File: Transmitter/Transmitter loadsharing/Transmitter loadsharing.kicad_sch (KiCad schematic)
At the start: 115 parts, among them J1 Conn_Coaxial, J10 Conn_01x01, J11 Conn_01x01, J12 Conn_01x01, J13 Conn_01x01, J14 Conn_01x01, J15 Conn_01x01, J16 Conn_01x01, J17 Conn_Coaxial, J18 Conn_Coaxial, J19 Conn_Coaxial, J2 Conn_01x03, J20 Conn_01x01, J21 Conn_01x01, J22 Conn_01x01, J23 Conn_01x01, J24 Conn_01x01, J25 Conn_01x01, J3 Conn_01x03, J4 Conn_01x02_Socket, J5 Conn_01x02, J6 Conn_01x01, J7 Conn_01x02, J8 Conn_01x02_Socket, J9 Conn_01x01, U1 OPA3692IDBQR, U10 LT3094EMSE-PBF, U11 LT3094EMSE-PBF, U2 THS3091D, U3 THS3091D, U4 THS3091D, U5 THS3091D, U6 THS3091D, U7 THS3091D, U8 LT3045EMSE-PBF, U9 LT3045EMSE-PBF

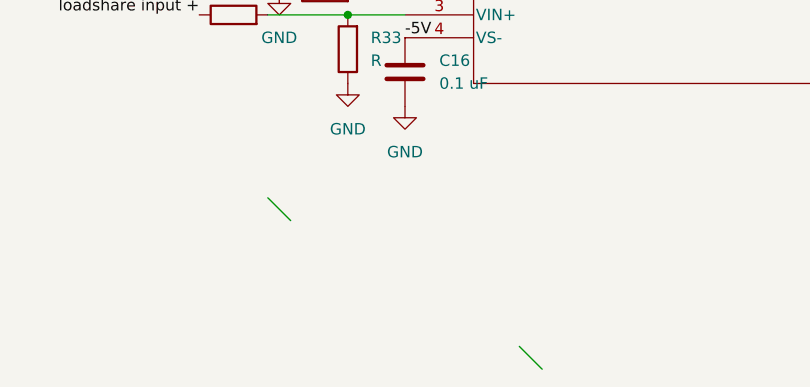
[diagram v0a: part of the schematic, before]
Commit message: Fixed spacing between ICs, tried to make traces the same length each of the loadsharing op-amps
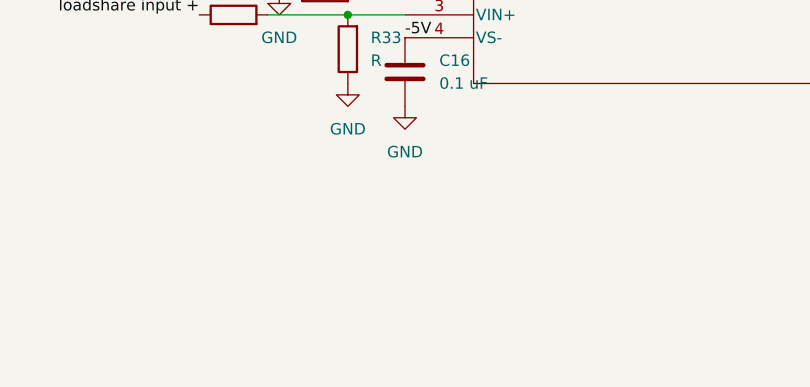
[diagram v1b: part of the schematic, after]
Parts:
- U2: footprint THS3091DDR:DDA8_2P28X2P28 -> D8
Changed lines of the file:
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@@
 		(at 336.55 107.95)
 	)
-	(bus_entry
-		(at 39.37 265.43)
-		(size 2.54 2.54)
-		(stroke
-			(width 0)
-			(type default)
-		)
-	)
-	(bus_entry
-		(at 67.31 281.94)
-		(size 2.54 2.54)
-		(stroke
-			(width 0)
-			(type default)
-		)
-	)
 	(wire
 		(pts
@@
 	)
 	(symbol
+		(lib_name "THS3091D_2")
 		(lib_id "THS3091:THS3091D")
 		(at 55.88 207.01 0)
@@
 	)
 	(symbol
+		(lib_name "THS3091D_5")
 		(lib_id "THS3091:THS3091D")
 		(at 209.55 208.28 0)
@@
 			)
 		)
-		(property "Footprint" "THS3091DDR:DDA8_2P28X2P28"
+		(property "Footprint" "D8"
 			(at 55.88 173.99 0)
 			(effects
@@
 	)
 	(symbol
+		(lib_name "THS3091D_3")
 		(lib_id "THS3091:THS3091D")
 		(at 54.61 240.03 0)
@@
 	)
 	(symbol
+		(lib_name "THS3091D_4")
 		(lib_id "THS3091:THS3091D")
 		(at 208.28 241.3 0)

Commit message: git being weird
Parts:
- C10, C14, C18, C2, C22, C3: value 6.8 uF -> 6.8uF
- C11, C12, C13, C15, C16, C17, C19, C20, C21, C23, C24, C25, C4: value 0.1 uF -> 0.1uF
- C26, C30: value 0.47u -> 0.47uF
- C27, C28, C31, C32, C9: value 10u -> 10uF
- C29: value 22u -> 22uF
- R10, R18, R19, R20, R4, R7: value R -> Ro
- R11, R21: value 1 Ohm -> 1Ω
- R12, R13, R14, R3, R5, R8: value 250 Ohm -> Rg
- R15, R16, R17, R2, R6, R9: value 1 kOhm -> Rf
- R22, R23: value R -> Rled
- R24, R25, R26, R3: value 50 Ohm -> 50Ω
- R29, R31, R33, R35, R37, R39: value R -> Rt
- R30, R32, R34, R36, R38: value 0 Ohm -> 0Ω
- U2: footprint D8 -> THS3091DDR:DDA8_2P28X2P28
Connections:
- net +5V_In is gone; now on net +5V: C27.1, C28.1, J2.1 (Pin_1), U8.10 (OUTS), U8.11 (OUT), U9.10 (OUTS), U9.11 (OUT)
- net -5V_In is gone; now on net -5V: C31.1, C32.1, J3.1 (Pin_1), U10.10 (OUTS), U10.11 (OUT), U11.10 (OUTS), U11.11 (OUT)
- net +5V: now also U8.12 (OUT), U9.12 (OUT)
- net -5V: now also U10.12 (OUT), U11.12 (OUT)
- net GND: no longer U10.13 (IN), U11.13 (IN)
- net PWR+: now also U8.2 (IN), U8.3 (IN), U9.2 (IN), U9.3 (IN)
- net PWR-: now also U10.13 (IN), U10.2 (IN), U11.13 (IN), U11.2 (IN)
- no-connect marks 39 -> 29

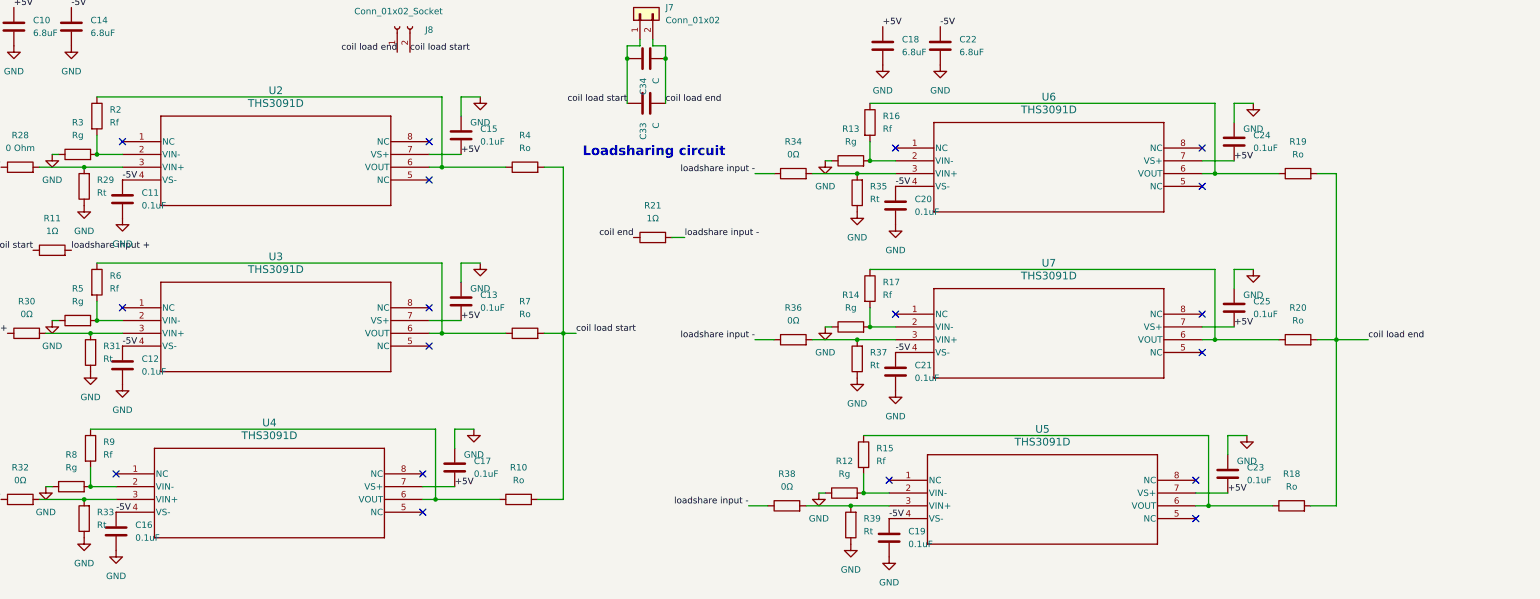
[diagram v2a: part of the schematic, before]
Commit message: Changed symbol for THS to add EPAD connection, fixed thermal vias on footprint, fixed THS3091 dir
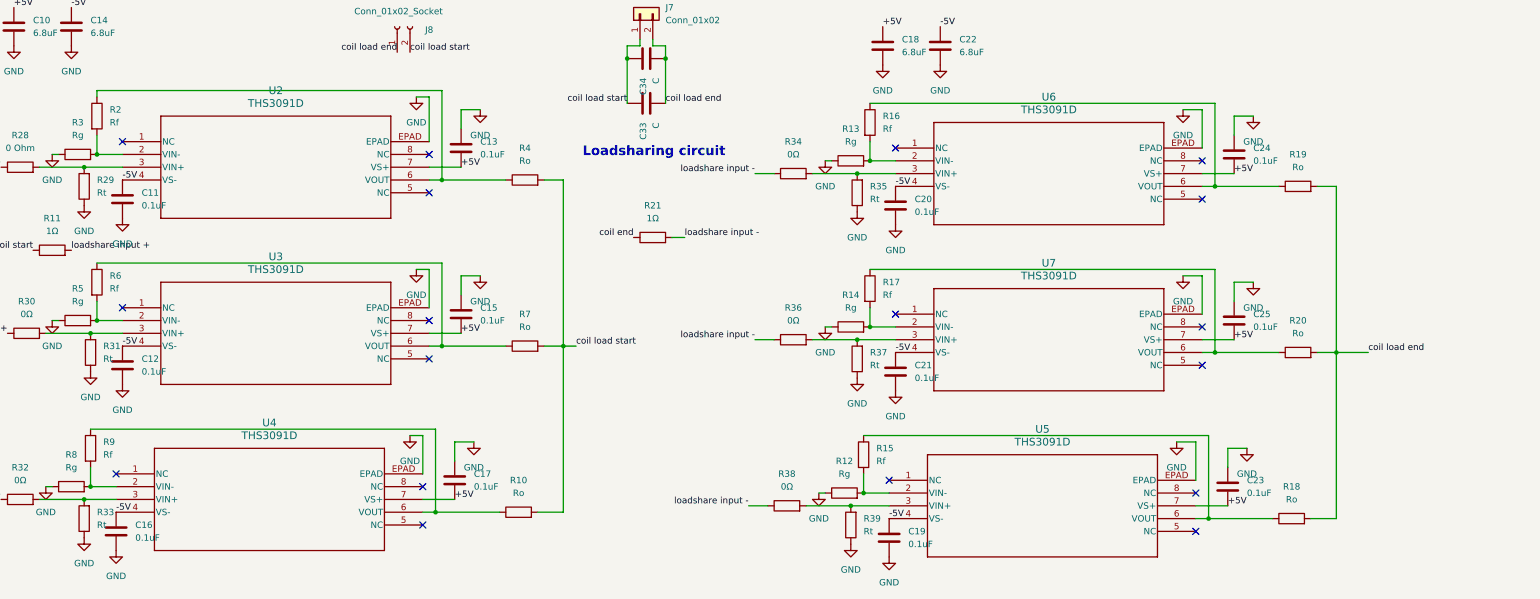
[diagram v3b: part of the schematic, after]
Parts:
- U2: symbol THS3091:THS3091D -> THS3091:THS3091DDA
- U3, U4, U5, U6, U7: footprint THS3091DDR:DDA8_2P28X2P28 -> DDA8_2P28X2P28; symbol THS3091:THS3091D -> THS3091:THS3091DDA
- renumbered C15 to C13, C13 to C15
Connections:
- net GND: now also U2.EPAD, U3.EPAD, U4.EPAD, U5.EPAD, U6.EPAD, U7.EPAD
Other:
- moved on the sheet: C13, C15, C17, C23, C24, C25, R10, R18, R19, R20, R4, R7

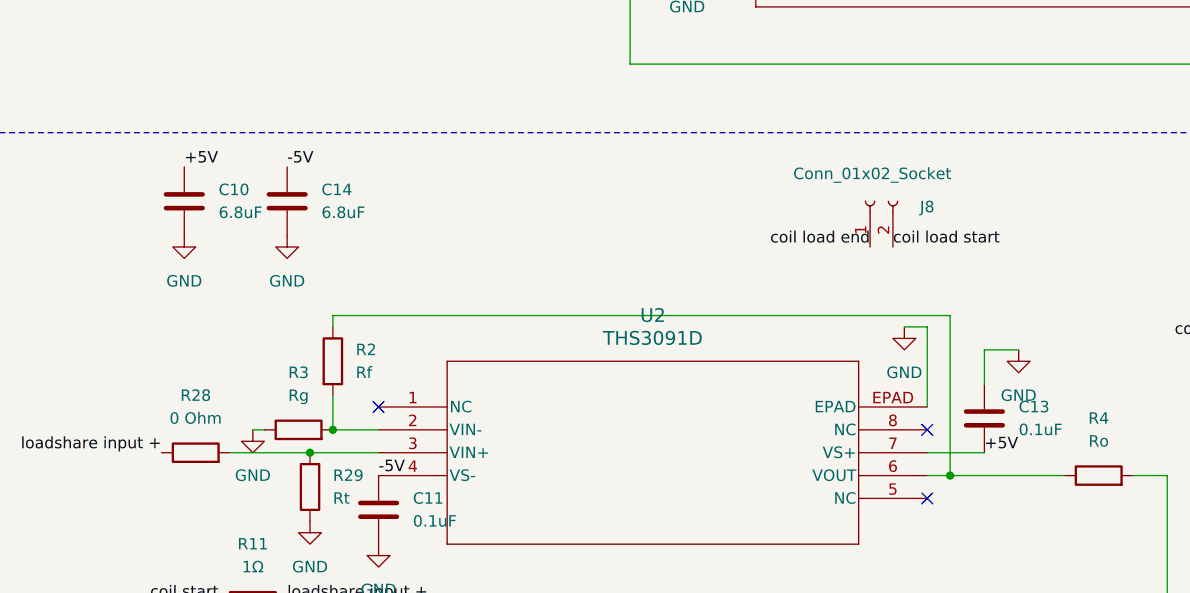
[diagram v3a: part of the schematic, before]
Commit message: Drew a footprint for a BNC edge connector 112640, made sure coils are centered and as symmetrical as possible:wq
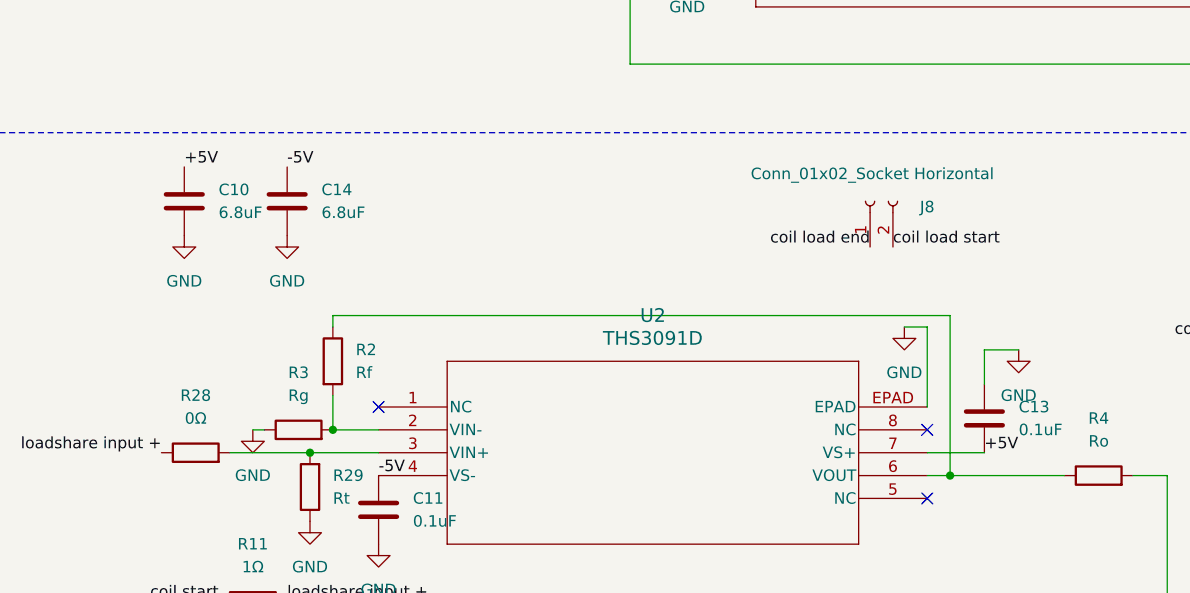
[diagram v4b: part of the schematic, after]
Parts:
- J8: value Conn_01x02_Socket -> Conn_01x02_Socket Horizontal
- R28: value 0 Ohm -> 0Ω
- U3, U4, U5, U6, U7: footprint DDA8_2P28X2P28 -> THS3091:DDA8_2P28X2P28
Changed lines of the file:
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@@
 			)
 		)
-		(property "Value" "Conn_01x02_Socket"
+		(property "Value" "Conn_01x02_Socket Horizontal"
 			(at 110.744 148.082 90)
 			(effects
@@
 			)
 		)
-		(property "Footprint" "DDA8_2P28X2P28"
+		(property "Footprint" "THS3091:DDA8_2P28X2P28"
 			(at 55.88 207.01 0)
 			(effects
@@
 			)
 		)
-		(property "Footprint" "DDA8_2P28X2P28"
+		(property "Footprint" "THS3091:DDA8_2P28X2P28"
 			(at 209.55 208.28 0)
 			(effects
@@
 			)
 		)
-		(property "Footprint" "DDA8_2P28X2P28"
+		(property "Footprint" "THS3091:DDA8_2P28X2P28"
 			(at 54.61 240.03 0)
 			(effects
@@
 			)
 		)
-		(property "Footprint" "DDA8_2P28X2P28"
+		(property "Footprint" "THS3091:DDA8_2P28X2P28"
 			(at 209.55 175.26 0)
 			(effects
@@
 			)
 		)
-		(property "Value" "0 Ohm"
+		(property "Value" "0Ω"
 			(at 35.56 175.26 90)
 			(effects
@@
 			)
 		)
-		(property "Footprint" "DDA8_2P28X2P28"
+		(property "Footprint" "THS3091:DDA8_2P28X2P28"
 			(at 208.28 241.3 0)
 			(effects

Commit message: Final version before review 3
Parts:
- J17, J18: footprint Connector_Coaxial:BNC_Amphenol_B6252HB-NPP3G-50_Horizontal -> BNc_Amphenol_112640:BNC_Amphenol_112640_Edge_mount
- U1: footprint Opa3692 SOIC:DBQ16 -> Opa3692 SSOP:DBQ16
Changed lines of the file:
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@@
 			)
 		)
-		(property "Footprint" "Connector_Coaxial:BNC_Amphenol_B6252HB-NPP3G-50_Horizontal"
+		(property "Footprint" "BNc_Amphenol_112640:BNC_Amphenol_112640_Edge_mount"
 			(at 320.04 21.59 0)
 			(effects
@@
 			)
 		)
-		(property "Footprint" "Connector_Coaxial:BNC_Amphenol_B6252HB-NPP3G-50_Horizontal"
+		(property "Footprint" "BNc_Amphenol_112640:BNC_Amphenol_112640_Edge_mount"
 			(at 233.68 20.32 0)
 			(effects
@@
 			)
 		)
-		(property "Footprint" "Opa3692 SOIC:DBQ16"
+		(property "Footprint" "Opa3692 SSOP:DBQ16"
 			(at 90.17 106.68 0)
 			(effects

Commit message: blurp
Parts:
- C30: value 0.47uF -> 4.7uF
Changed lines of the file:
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@@
 			)
 		)
-		(property "Value" "0.47uF"
+		(property "Value" "4.7uF"
 			(at 377.19 128.27 0)
 			(effects

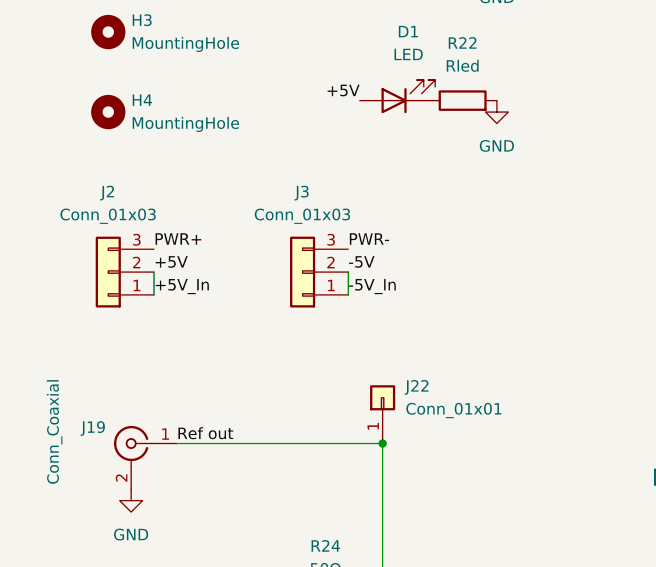
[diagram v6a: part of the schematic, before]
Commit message: Fixed shorting of +-5V_In and +-5V nets
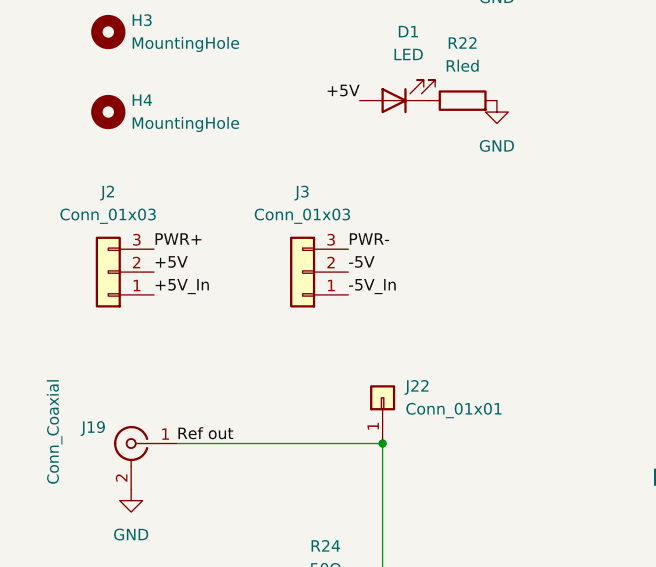
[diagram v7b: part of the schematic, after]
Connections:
- net +5V: no longer C27.1, C28.1, J2.1 (Pin_1), U8.10 (OUTS), U8.11 (OUT), U8.12 (OUT), U9.10 (OUTS), U9.11 (OUT), U9.12 (OUT)
- net -5V: no longer C31.1, C32.1, J3.1 (Pin_1), U10.10 (OUTS), U10.11 (OUT), U10.12 (OUT), U11.10 (OUTS), U11.11 (OUT), U11.12 (OUT)
- new net +5V_In: C27.1, C28.1, J2.1 (Pin_1), U8.10 (OUTS), U8.11 (OUT), U8.12 (OUT), U9.10 (OUTS), U9.11 (OUT), U9.12 (OUT)
- new net -5V_In: C31.1, C32.1, J3.1 (Pin_1), U10.10 (OUTS), U10.11 (OUT), U10.12 (OUT), U11.10 (OUTS), U11.11 (OUT), U11.12 (OUT)
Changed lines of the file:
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@@
-	(wire
-		(pts
-			(xy 46.99 64.77) (xy 46.99 67.31)
-		)
-		(stroke
-			(width 0)
-			(type default)
-		)
-	)
 	(wire
 		(pts
@@
 		)
 		(stroke
-			(width 0)
-			(type default)
-		)
-	)
-	(wire
-		(pts
-			(xy 25.4 64.77) (xy 25.4 67.31)
-		)
-		(stroke
